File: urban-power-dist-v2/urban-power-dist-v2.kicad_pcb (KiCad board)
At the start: 2 copper layers, 22 parts, among them J1 12V_IN, J2 FRONT_ACC_OUT, J3 REAR_ACC_OUT, J4 TEL_OUT, J5 TEST_PT_1, J6 TEST_PT_2, J7 TEST_PT_3

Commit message: With hierarchical sheets
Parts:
- removed D4, D5: LED, LED_SMD:LED_0603_1608Metric_Pad1.05x0.95mm_HandSolder
- removed F2: REAR_ACC_FUSE, Fuse:Fuseholder_Blade_Mini_Keystone_3568
- removed F3: TEL_FUSE, Fuse:Fuseholder_Blade_Mini_Keystone_3568
- removed J3: REAR_ACC_OUT, ATF13-2P-BM03:ATF132PBM03
- removed J4: TEL_OUT, ATF13-2P-BM03:ATF132PBM03
- removed J6: TEST_PT_2, Connector_PinHeader_2.54mm:PinHeader_1x03_P2.54mm_Vertical
- removed J7: TEST_PT_3, Connector_PinHeader_2.54mm:PinHeader_1x03_P2.54mm_Vertical
- removed R3, R4: 9.45K, Resistor_SMD:R_1206_3216Metric_Pad1.30x1.75mm_HandSolder
- removed R6, R7: 0.01R, Resistor_SMD:R_0805_2012Metric_Pad1.20x1.40mm_HandSolder
- added D6: LED, LED_SMD:LED_0603_1608Metric_Pad1.05x0.95mm_HandSolder, F.Cu at (91.3, 68.2)
- added D7: LED, LED_SMD:LED_0603_1608Metric_Pad1.05x0.95mm_HandSolder, F.Cu at (123.7, 136.5)
- added F4: FUSE, Fuse:Fuseholder_Blade_Mini_Keystone_3568, F.Cu at (69.4, 69.3)
- added F5: FUSE, Fuse:Fuseholder_Blade_Mini_Keystone_3568, F.Cu at (101.8, 137.7)
- added J10: TEST_PT, Connector_PinHeader_2.54mm:PinHeader_1x03_P2.54mm_Vertical, F.Cu at (128.1, 102.7)
- added J11: OUT, ATF13-2P-BM03:ATF132PBM03, F.Cu at (109.2, 107.9)
- added J8: TEST_PT, Connector_PinHeader_2.54mm:PinHeader_1x03_P2.54mm_Vertical, F.Cu at (95.7, 34.4)
- added J9: OUT, ATF13-2P-BM03:ATF132PBM03, F.Cu at (76.8, 39.5)
- added R10: 0.01R, Resistor_SMD:R_0805_2012Metric_Pad1.20x1.40mm_HandSolder, F.Cu at (117.9, 140.0)
- added R11: 9.45K, Resistor_SMD:R_1206_3216Metric_Pad1.30x1.75mm_HandSolder, F.Cu at (118.5, 136.9)
- added R8: 0.01R, Resistor_SMD:R_0805_2012Metric_Pad1.20x1.40mm_HandSolder, F.Cu at (85.5, 71.7)
- added R9: 9.45K, Resistor_SMD:R_1206_3216Metric_Pad1.30x1.75mm_HandSolder, F.Cu at (86.1, 68.6)
- F1: value FRONT_ACC_FUSE -> FUSE
- J2: value FRONT_ACC_OUT -> TEST_PT; footprint ATF13-2P-BM03:ATF132PBM03 -> Connector_PinHeader_2.54mm:PinHeader_1x03_P2.54mm_Vertical
- J5: value TEST_PT_1 -> OUT; footprint Connector_PinHeader_2.54mm:PinHeader_1x03_P2.54mm_Vertical -> ATF13-2P-BM03:ATF132PBM03
- R2: value 9.45K -> 0.01R; footprint Resistor_SMD:R_1206_3216Metric_Pad1.30x1.75mm_HandSolder -> Resistor_SMD:R_0805_2012Metric_Pad1.20x1.40mm_HandSolder
- R5: value 0.01R -> 9.45K; footprint Resistor_SMD:R_0805_2012Metric_Pad1.20x1.40mm_HandSolder -> Resistor_SMD:R_1206_3216Metric_Pad1.30x1.75mm_HandSolder
- moved J1 145.2 mm to (204.8, 90.0)
- moved F1 82.4 mm to (136.2, 92.6)
- moved R1 78.9 mm to (183.5, 81.5)
- moved D2 73.1 mm to (189.6, 96.5)
- moved J5 55.0 mm to (143.7, 62.8)
- moved D1 54.3 mm to (180.0, 114.0)
- moved D3 49.6 mm to (158.1, 91.4)
- moved R2 47.6 mm to (152.3, 94.9)
- moved J2 37.1 mm to (162.6, 57.6)
- moved R5 30.7 mm to (152.9, 91.8)
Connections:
- F1 pad 2: Net-(J5-Pin_1) -> Net-(J2-Pin_1)
- J2 pad 2: GND -> Net-(J2-Pin_2)
- J5 pad 1: Net-(J5-Pin_1) -> Net-(J2-Pin_2)
- J5 pad 2: Net-(J2-Pin_1) -> GND
- R2 pad 1: Net-(D3-A) -> Net-(J2-Pin_1)
- R2 pad 2: Net-(J2-Pin_1) -> Net-(J2-Pin_2)
- R5 pad 1: Net-(J5-Pin_1) -> Net-(D3-A)
- R5 pad 2: Net-(J2-Pin_1) -> Net-(J2-Pin_2)

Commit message: pcb layout
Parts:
- removed D6, D7: LED, LED_SMD:LED_0603_1608Metric_Pad1.05x0.95mm_HandSolder
- removed F4, F5: FUSE, Fuse:Fuseholder_Blade_Mini_Keystone_3568
- removed J10, J8: TEST_PT, Connector_PinHeader_2.54mm:PinHeader_1x03_P2.54mm_Vertical
- removed J11, J9: OUT, ATF13-2P-BM03:ATF132PBM03
- removed R10, R8: 0.01R, Resistor_SMD:R_0805_2012Metric_Pad1.20x1.40mm_HandSolder
- removed R11, R9: 9.45K, Resistor_SMD:R_1206_3216Metric_Pad1.30x1.75mm_HandSolder
- added D4: LED, LED_SMD:LED_0603_1608Metric_Pad1.05x0.95mm_HandSolder, F.Cu at (171.7, 68.5)
- added D5: LED, LED_SMD:LED_0603_1608Metric_Pad1.05x0.95mm_HandSolder, F.Cu at (215.0, 96.4)
- added F2: FUSE, Fuse:Fuseholder_Blade_Mini_Keystone_3568, F.Cu at (132.8, 78.5)
- added F3: FUSE, Fuse:Fuseholder_Blade_Mini_Keystone_3568, F.Cu at (205.0, 57.5)
- added G***: LOGO, LOGO, F.Cu at (47.8, 27.2)
- added J3: OUT, ATF13-2P-BM03:ATF132PBM03, F.Cu at (162.0, 48.0)
- added J4: OUT, ATF13-2P-BM03:ATF132PBM03, F.Cu at (235.6, 86.7)
- added J6: TEST_PT, Connector_PinHeader_2.54mm:PinHeader_1x03_P2.54mm_Vertical, F.Cu at (165.8, 88.0)
- added J7: TEST_PT, Connector_PinHeader_2.54mm:PinHeader_1x03_P2.54mm_Vertical, F.Cu at (195.5, 90.5)
- added R3: 9.45K, Resistor_SMD:R_1206_3216Metric_Pad1.30x1.75mm_HandSolder, F.Cu at (162.8, 68.5)
- added R4: 9.45K, Resistor_SMD:R_1206_3216Metric_Pad1.30x1.75mm_HandSolder, F.Cu at (215.0, 87.5)
- added R6: 0.01R, Resistor_SMD:R_0805_2012Metric_Pad1.20x1.40mm_HandSolder, F.Cu at (147.3, 68.5)
- added R7: 0.01R, Resistor_SMD:R_0805_2012Metric_Pad1.20x1.40mm_HandSolder, F.Cu at (215.0, 72.0)
- J2: value TEST_PT -> OUT; footprint Connector_PinHeader_2.54mm:PinHeader_1x03_P2.54mm_Vertical -> ATF13-2P-BM03:ATF132PBM03
- J5: value OUT -> TEST_PT; footprint ATF13-2P-BM03:ATF132PBM03 -> Connector_PinHeader_2.54mm:PinHeader_1x03_P2.54mm_Vertical
- R2: value 0.01R -> 9.45K; footprint Resistor_SMD:R_0805_2012Metric_Pad1.20x1.40mm_HandSolder -> Resistor_SMD:R_1206_3216Metric_Pad1.30x1.75mm_HandSolder
- R5: value 9.45K -> 0.01R; footprint Resistor_SMD:R_1206_3216Metric_Pad1.30x1.75mm_HandSolder -> Resistor_SMD:R_0805_2012Metric_Pad1.20x1.40mm_HandSolder
- moved J2 99.3 mm to (66.5, 82.3), turned to -90 degrees
- moved D3 73.6 mm to (87.0, 72.6), turned to 90 degrees
- moved R2 66.7 mm to (87.0, 81.5), turned to 90 degrees
- moved R5 66.2 mm to (87.0, 97.0), turned to 90 degrees
- moved J1 65.5 mm to (151.8, 128.6)
- moved D2 43.8 mm to (147.4, 108.5)
- moved F1 43.6 mm to (97.0, 111.5), turned to 180 degrees
- moved J5 40.4 mm to (106.5, 78.5), turned to 180 degrees
- moved R1 36.2 mm to (159.4, 108.5)
- moved D1 28.1 mm to (151.9, 115.5)
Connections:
- F1 pad 2: Net-(J2-Pin_1) -> Net-(J5-Pin_1)
- J2 pad 2: Net-(J2-Pin_2) -> GND
- J5 pad 1: Net-(J2-Pin_2) -> Net-(J5-Pin_1)
- J5 pad 2: GND -> Net-(J2-Pin_1)
- R2 pad 1: Net-(J2-Pin_1) -> Net-(D3-A)
- R2 pad 2: Net-(J2-Pin_2) -> Net-(J2-Pin_1)
- R5 pad 1: Net-(D3-A) -> Net-(J5-Pin_1)
- R5 pad 2: Net-(J2-Pin_2) -> Net-(J2-Pin_1)
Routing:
- added copper zone on B.Cu, net GND

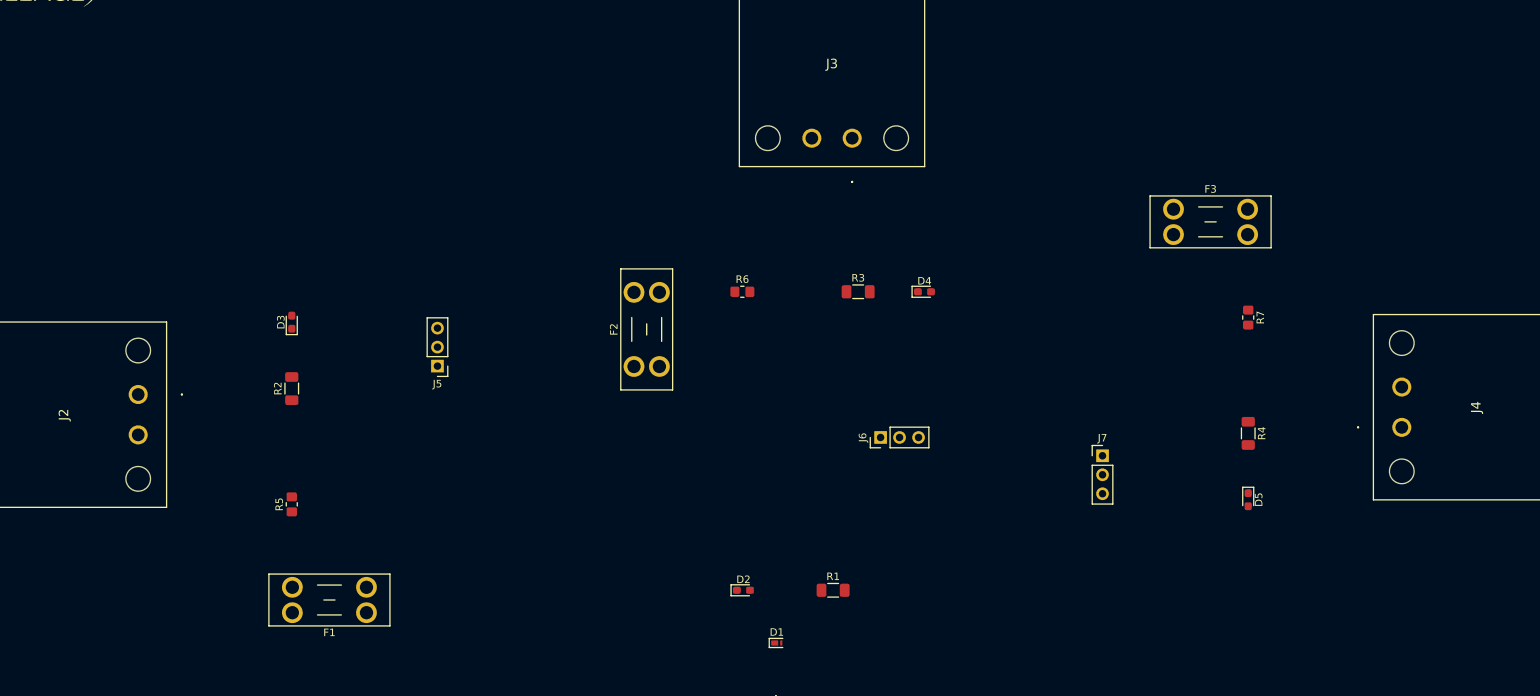
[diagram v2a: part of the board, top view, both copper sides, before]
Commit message: update tvs diode, layout changes
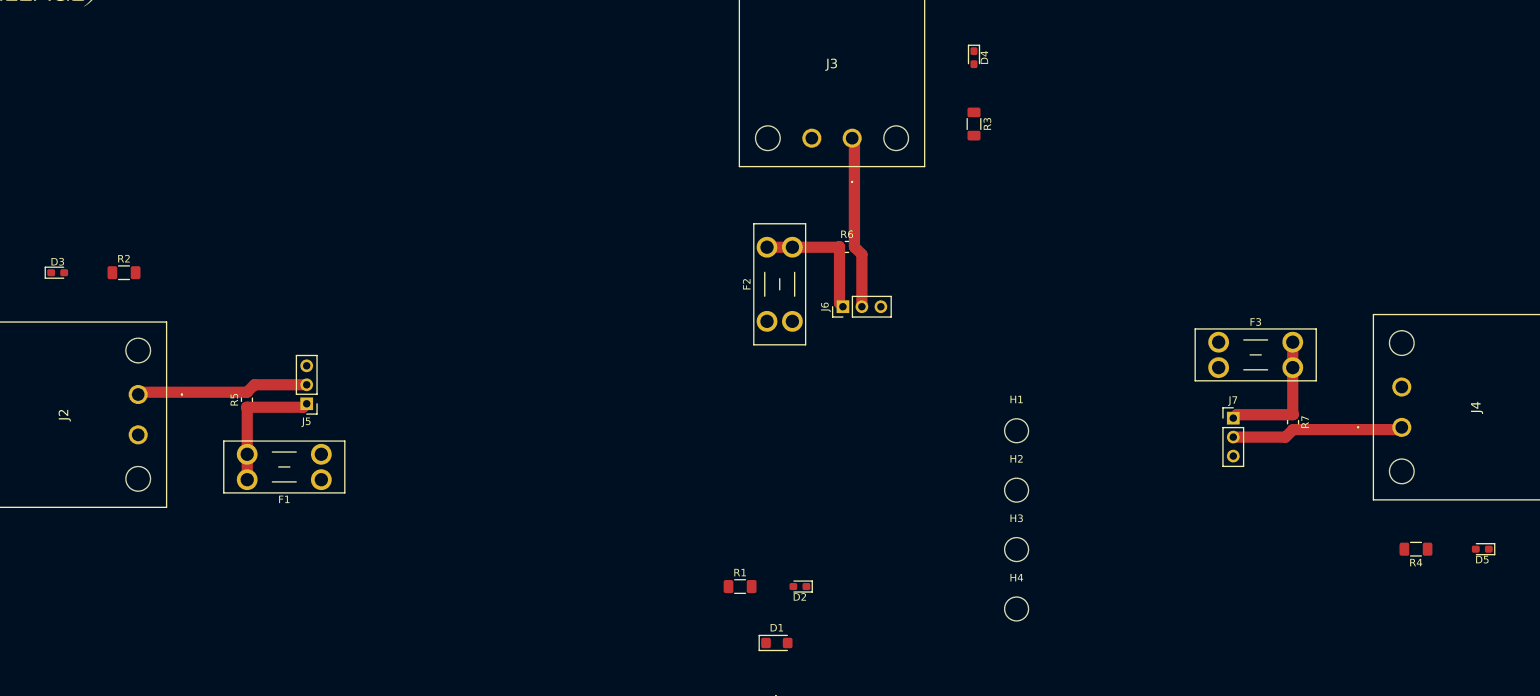
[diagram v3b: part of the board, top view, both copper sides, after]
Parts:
- added H1: MountingHole, MountingHole:MountingHole_3.2mm_M3, F.Cu at (184.0, 87.2)
- added H2: MountingHole, MountingHole:MountingHole_3.2mm_M3, F.Cu at (184.0, 95.1)
- added H3: MountingHole, MountingHole:MountingHole_3.2mm_M3, F.Cu at (184.0, 103.0)
- added H4: MountingHole, MountingHole:MountingHole_3.2mm_M3, F.Cu at (184.0, 111.0)
- D1: footprint Diode_SMD:Nexperia_DSN1608-2_1.6x0.8mm -> Diode_SMD:D_SMF
- moved D3 32.0 mm to (55.7, 66.0), turned to 0 degrees
- moved D4 32.0 mm to (178.3, 37.2), turned to -90 degrees
- moved D5 32.0 mm to (246.3, 103.0), turned to 180 degrees
- moved R2 27.3 mm to (64.5, 66.0), turned to 0 degrees
- moved R3 27.3 mm to (178.3, 46.1), turned to -90 degrees
- moved R4 27.3 mm to (237.4, 103.0), turned to 180 degrees
- moved F1 18.8 mm to (91.0, 93.7)
- moved F2 18.8 mm to (150.6, 72.5)
- moved F3 18.8 mm to (211.0, 75.3)
- moved J5 18.2 mm to (89.0, 83.5)
- moved J6 18.2 mm to (160.8, 70.5)
- moved J7 18.2 mm to (213.0, 85.5)
- moved R5 15.2 mm to (81.0, 83.0)
- moved R7 15.2 mm to (221.0, 86.0)
- moved R6 15.2 mm to (161.3, 62.5)
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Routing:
- net Net-(J4-Pin_1): track 0.00 -> 23.1 mm
- net Net-(J3-Pin_1): track 0.00 -> 23.1 mm
- net Net-(J2-Pin_1): track 0.00 -> 23.1 mm
- net Net-(J6-Pin_1): track 0.00 -> 17.9 mm
- net Net-(J5-Pin_1): track 0.00 -> 17.9 mm
- net Net-(J7-Pin_1): track 0.00 -> 17.9 mm

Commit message: layout updates
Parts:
- moved H1 129.0 mm to (75.5, 157.0)
- moved H2 120.4 mm to (75.5, 43.0)
- moved D3 100.7 mm to (156.0, 75.1), turned to 90 degrees
- moved J2 97.2 mm to (157.2, 47.5), turned to 180 degrees
- moved J4 96.2 mm to (151.8, 134.1), turned to 0 degrees
- moved D5 93.4 mm to (153.0, 106.4), turned to -90 degrees
- moved H3 93.0 mm to (236.0, 26.0)
- moved R2 91.5 mm to (156.0, 67.0), turned to 90 degrees
- moved R4 85.2 mm to (153.0, 114.5), turned to -90 degrees
- moved R5 78.0 mm to (155.0, 58.5), turned to 0 degrees
- moved R7 76.5 mm to (154.0, 123.0), turned to 180 degrees
- moved H4 68.4 mm to (236.0, 155.5)
- moved J3 67.5 mm to (212.6, 92.7), turned to 90 degrees
- moved J1 67.4 mm to (98.5, 87.3), turned to -90 degrees
- moved F3 57.3 mm to (166.2, 111.0), turned to -90 degrees
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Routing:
- net Net-(J6-Pin_1): track 17.9 -> 49.1 mm
- net Net-(J7-Pin_1): track 17.9 -> 49.1 mm
- net +12V: track 0.00 -> 30.6 mm
- net GND: track 0.00 -> 28.9 mm
- net Net-(J5-Pin_1): track 17.9 -> 35.5 mm
- net Net-(J4-Pin_1): track 23.1 -> 37.8 mm
- net Net-(J3-Pin_1): track 23.1 -> 37.8 mm
- net Net-(J2-Pin_1): track 23.1 -> 37.4 mm
- net Net-(D5-A): track 0.00 -> 5.70 mm
- net Net-(D3-A): track 0.00 -> 5.70 mm
- net Net-(D4-A): track 0.00 -> 5.70 mm
- removed copper zone on B.Cu, net GND
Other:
- board text added: "${REFERENCE}"

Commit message: close to finished layout
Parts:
- moved G*** 40.9 mm to (121.5, 47.0)
- moved H1 22.3 mm to (90.0, 140.0)
- moved F1 22.3 mm to (165.0, 72.9)
- moved F2 20.0 mm to (191.1, 98.2)
- moved H4 19.6 mm to (224.0, 140.0)
- moved H3 18.4 mm to (224.0, 40.0)
- moved F3 17.6 mm to (149.0, 107.1)
- moved J5 17.6 mm to (160.5, 80.0), turned to -90 degrees
- moved J6 15.8 mm to (184.0, 93.7), turned to 180 degrees
- moved H2 14.8 mm to (90.0, 40.0)
- moved J7 12.7 mm to (153.5, 100.0), turned to 90 degrees
- moved R1 11.3 mm to (128.2, 92.4), turned to 180 degrees
- moved D4 8.22 mm to (191.9, 87.2)
- moved R3 8.22 mm to (200.0, 87.2)
- moved D5 7.16 mm to (160.0, 107.9)
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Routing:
- net +12V: track 30.6 -> 0.00 mm
- net Net-(J6-Pin_1): track 49.1 -> 24.6 mm
- net Net-(J7-Pin_1): track 49.1 -> 24.6 mm
- net GND: track 28.9 -> 41.8 mm
- net Net-(J5-Pin_1): track 35.5 -> 24.6 mm
- net Net-(D2-A): track 0.00 -> 4.57 mm
- net Net-(J4-Pin_1): track 37.8 -> 34.8 mm
- net Net-(J3-Pin_1): track 37.8 -> 34.8 mm
- net Net-(J2-Pin_1): track 37.4 -> 34.8 mm
- added copper zone on F.Cu, net +12V
- added copper zone on B.Cu, net GND
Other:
- board outline added: 164 x 130 mm
- board text added: "BOARD NAME Aaron L, Samantha S SEMA 2026"

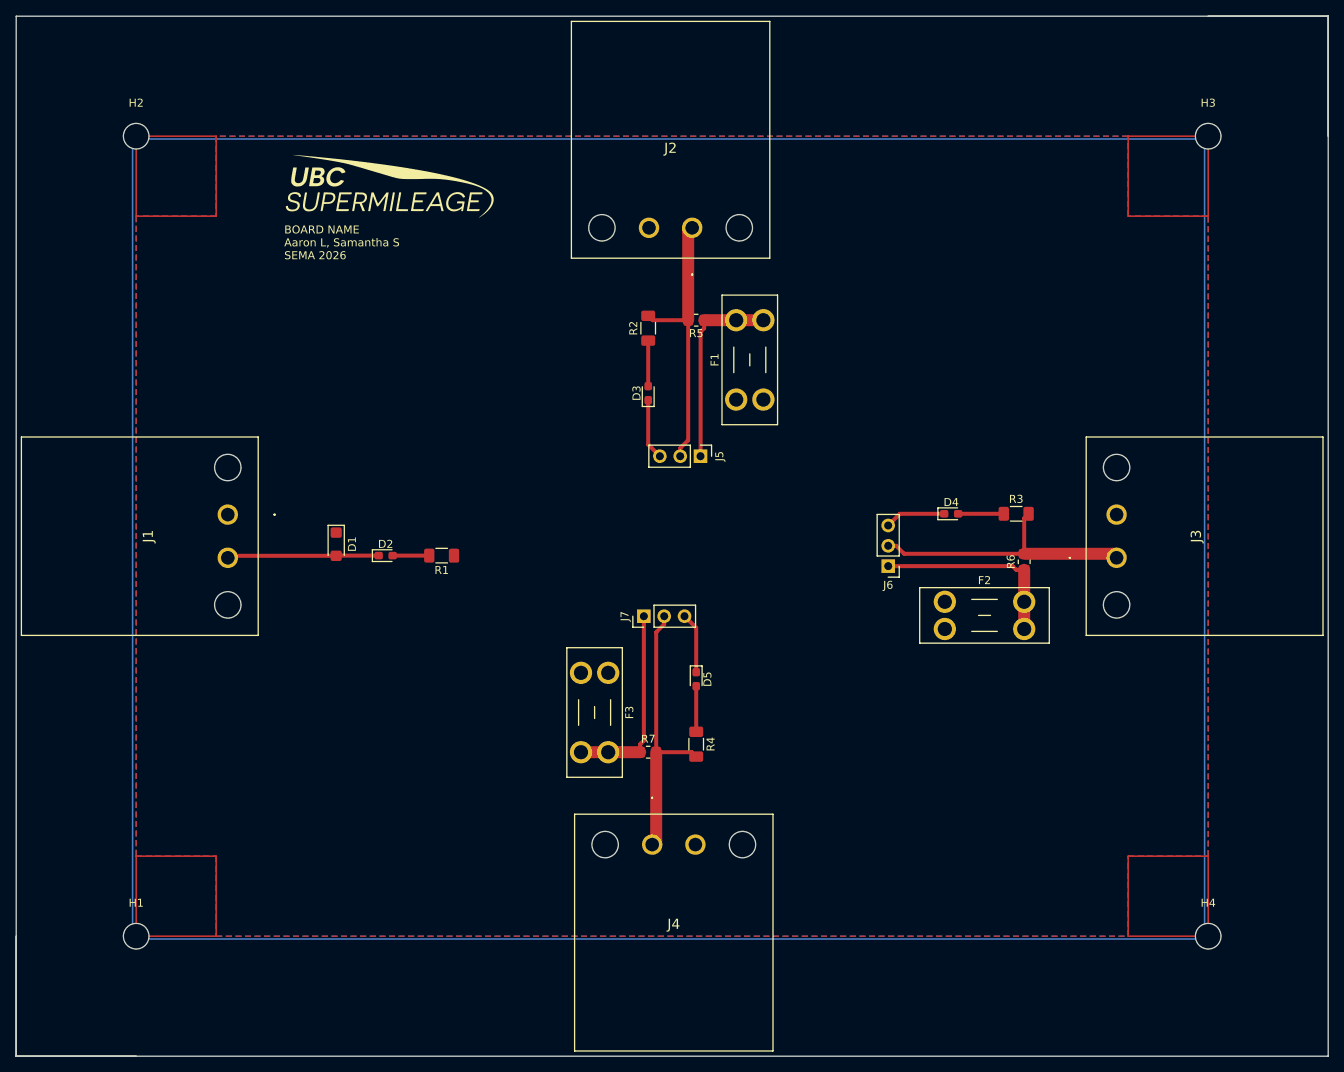
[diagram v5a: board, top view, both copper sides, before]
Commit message: layout DRC fixes
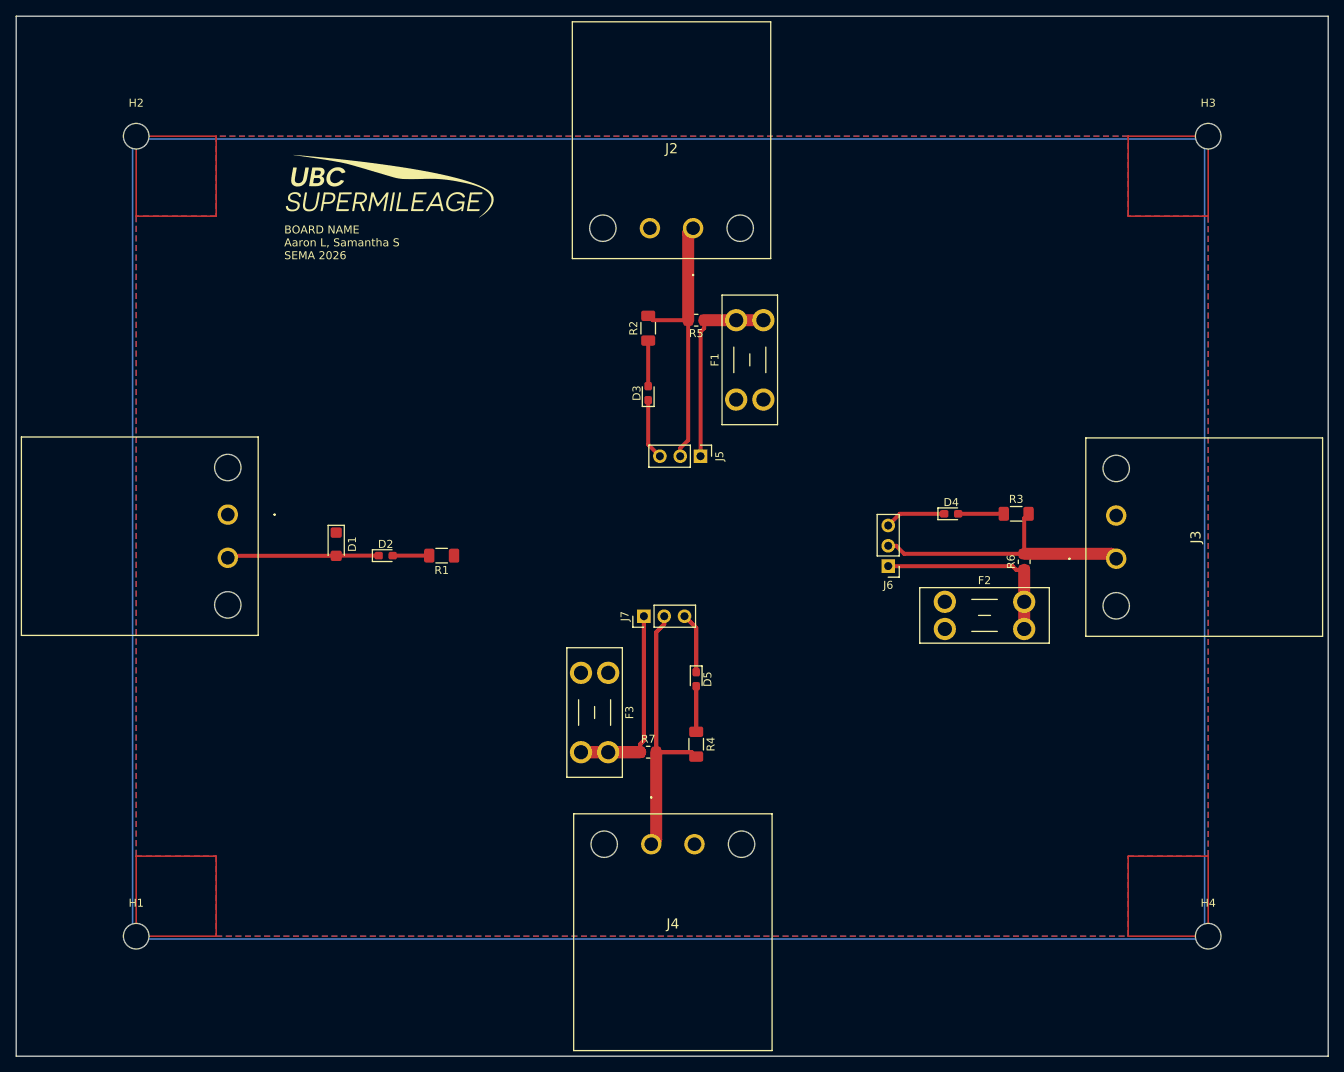
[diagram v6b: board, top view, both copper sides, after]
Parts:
- moved J4 0.13 mm to (154.4, 128.5)
- moved J2 0.13 mm to (159.6, 51.5)
- moved J3 0.13 mm to (212.5, 92.8)
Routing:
- net Net-(J7-Pin_1): track 24.6 -> 49.2 mm
- net Net-(J4-Pin_1): track 34.8 -> 57.0 mm
- net GND: track 41.8 -> 49.4 mm
- net Net-(D5-A): track 5.70 -> 11.4 mm
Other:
- outline, holes or cut-outs redrawn
- board text removed: "${REFERENCE}"
